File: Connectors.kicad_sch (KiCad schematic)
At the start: 20 parts, among them J16 USB_A_Stacked, J22 HR911130A, J23 HR911130A, J24 HR911130A, U1 TPS2065CDBV

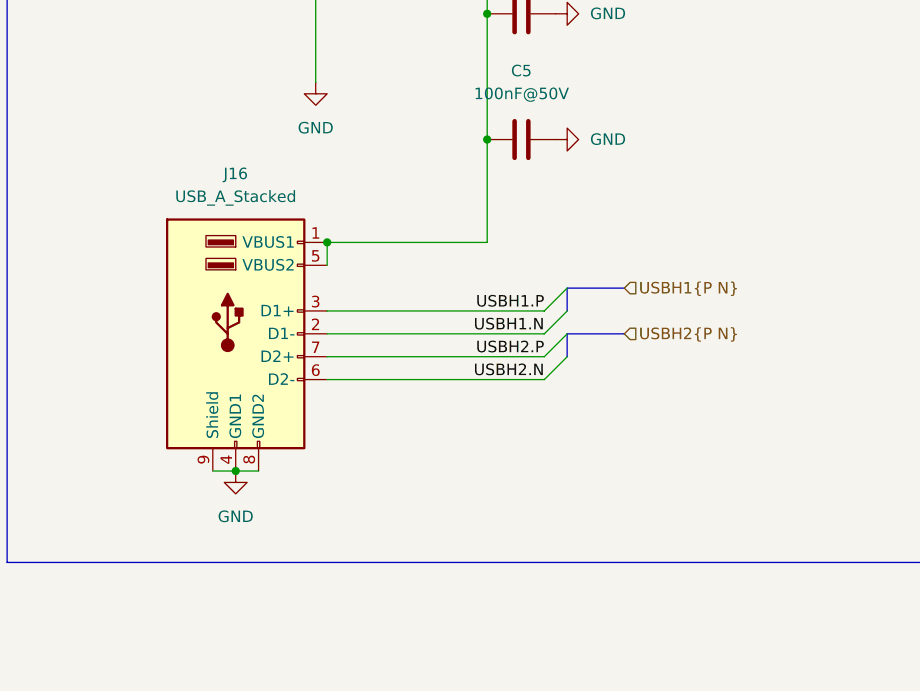
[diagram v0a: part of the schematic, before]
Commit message: Replaced stacked USB-A header with a single one (Fixes #15)
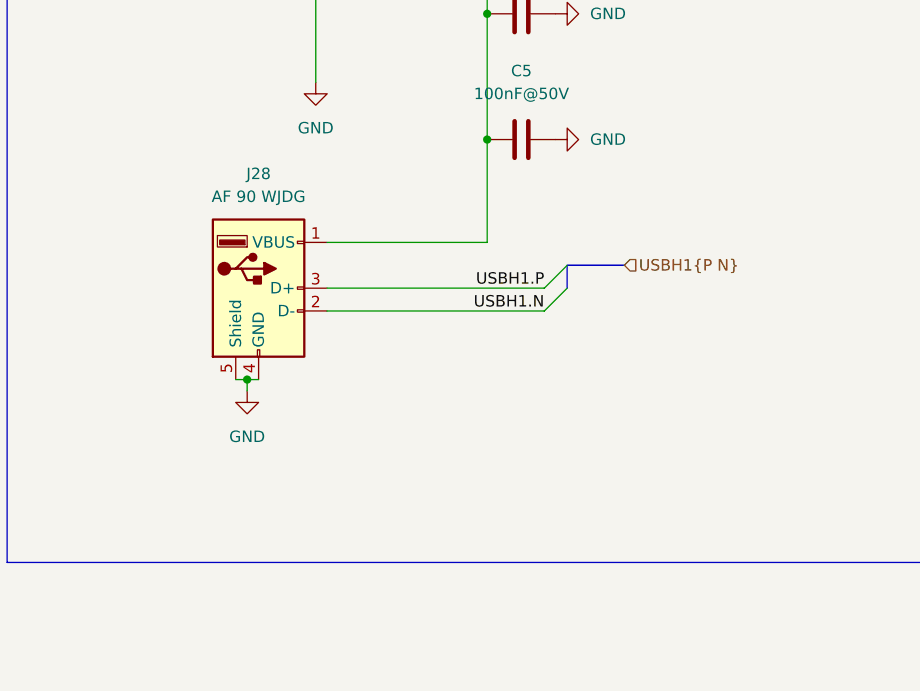
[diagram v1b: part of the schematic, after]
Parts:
- removed J16: USB_A_Stacked, nlbn:USB-269-BRW_C720548_MOD, symbol Connector:USB_A_Stacked
- added J28: AF 90 WJDG, Connector_USB:USB_A_Molex_67643_Horizontal, symbol Connector:USB_A
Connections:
- net GND: now also J28.4 (GND), J28.5 (Shield)
- net USBH1.N: now also J28.2 (D-)
- net USBH1.P: now also J28.3 (D+)
- net at C3.1, C4.1, C5.2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: now also J28.1 (VBUS)
